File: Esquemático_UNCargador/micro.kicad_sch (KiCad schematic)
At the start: 14 parts, among them J2 Relay, Q1 PN2222A, Q2 PN2222A

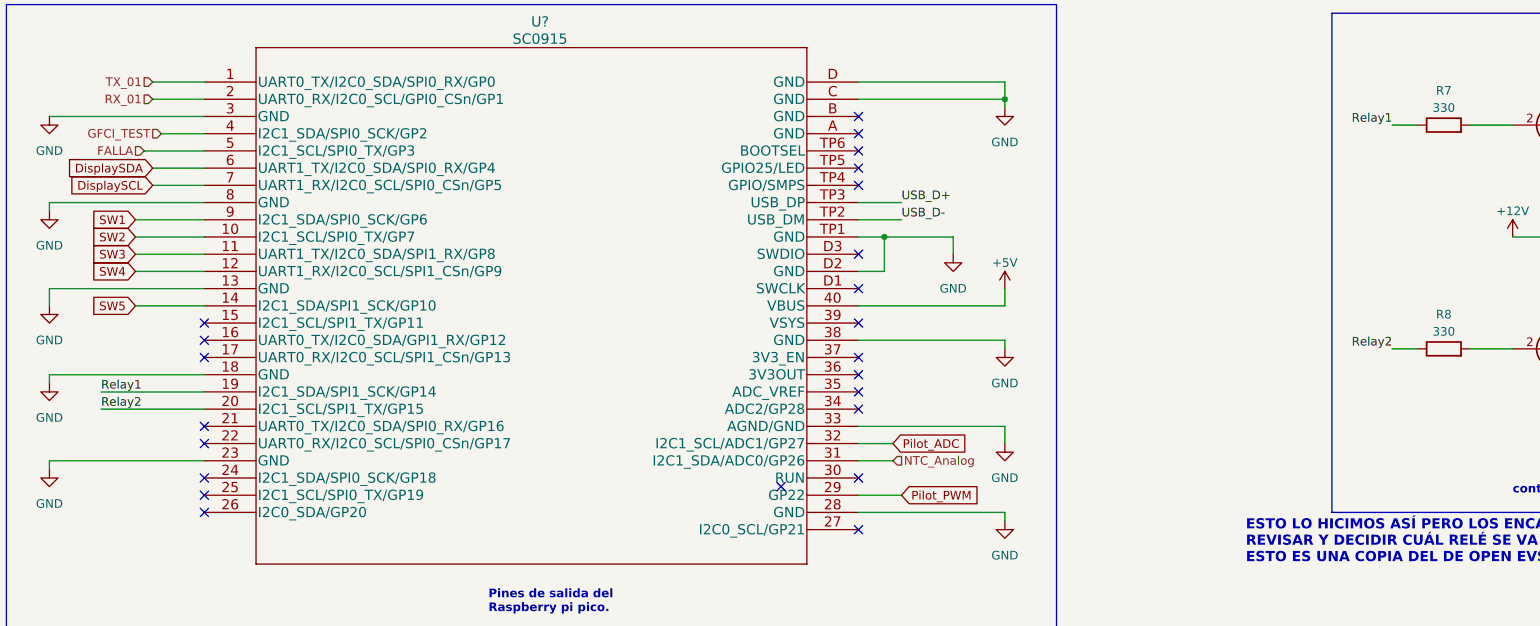
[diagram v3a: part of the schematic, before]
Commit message: Avances en Huellas
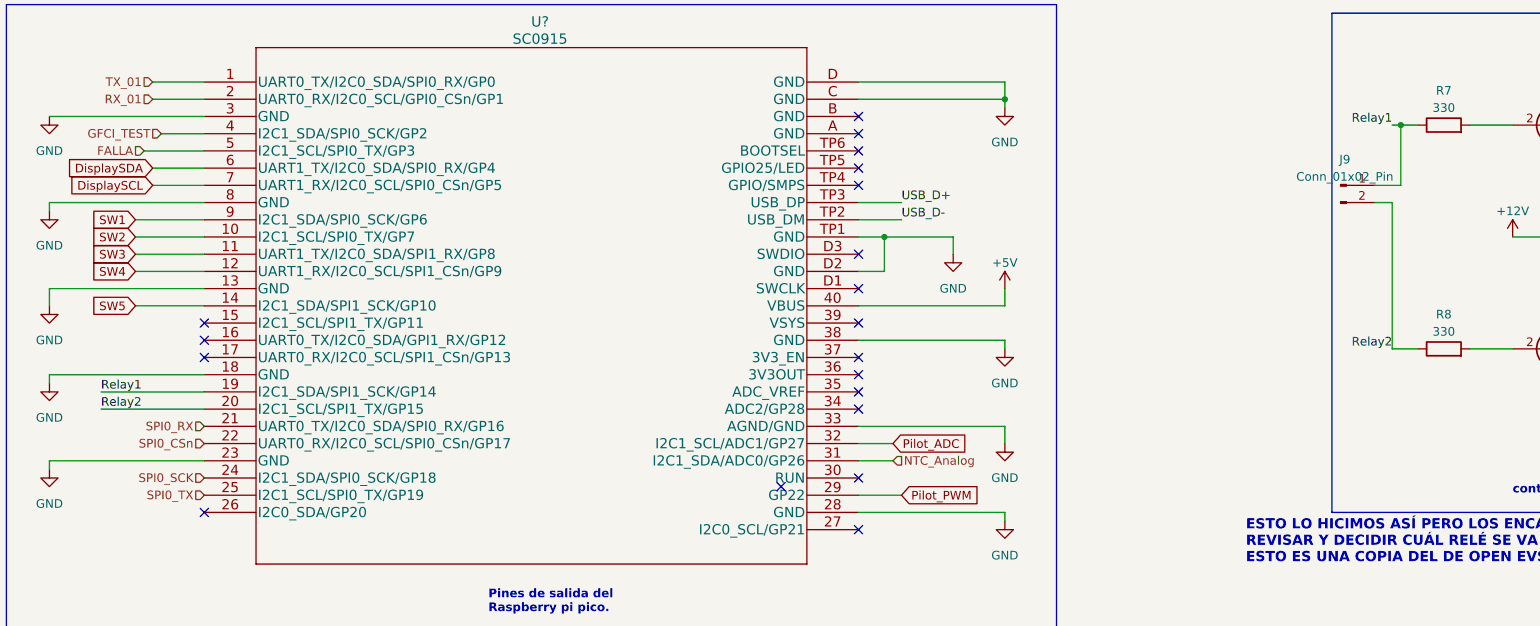
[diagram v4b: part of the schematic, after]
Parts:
- added J9: Conn_01x02_Pin, symbol Connector:Conn_01x02_Pin
- R7, R8: footprint (none) -> Resistor_THT:R_Axial_DIN0204_L3.6mm_D1.6mm_P5.08mm_Horizontal
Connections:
- net Relay1: now also J9.1 (Pin_1)
- net Relay2: now also J9.2 (Pin_2)
- net SPI0_RX: now reaches U?.21 (UART0_TX/I2C0_SDA/SPI0_RX/GP16)
- net SPI0_CSn: now reaches U?.22 (UART0_RX/I2C0_SCL/SPI0_CSn/GP17)
- net SPI0_SCK: now reaches U?.24 (I2C1_SDA/SPI0_SCK/GP18)
- net SPI0_TX: now reaches U?.25 (I2C1_SCL/SPI0_TX/GP19)
- no-connect marks 23 -> 19
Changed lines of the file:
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@@
   (junction (at 153.67 58.42) (diameter 0) (color 0 0 0 0)
+  )
+  (junction (at 229.87 41.91) (diameter 0) (color 0 0 0 0)
   )
   (junction (at 254 48.26) (diameter 0) (color 0 0 0 0)
@@
   (no_connect (at 149.86 48.26))
   (no_connect (at 53.34 76.2))
-  (no_connect (at 53.34 88.9))
   (no_connect (at 149.86 78.74))
   (no_connect (at 149.86 40.64))
   (no_connect (at 149.86 66.04))
   (no_connect (at 149.86 83.82))
-  (no_connect (at 53.34 86.36))
   (no_connect (at 149.86 76.2))
   (no_connect (at 149.86 81.28))
   (no_connect (at 53.34 99.06))
   (no_connect (at 149.86 60.96))
-  (no_connect (at 53.34 96.52))
   (no_connect (at 149.86 45.72))
   (no_connect (at 149.86 101.6))
@@
   (no_connect (at 149.86 50.8))
   (no_connect (at 149.86 93.98))
-  (no_connect (at 53.34 93.98))
   (no_connect (at 53.34 73.66))
   (no_connect (at 149.86 71.12))
@@
     (stroke (width 0) (type default))
   )
+  (wire (pts (xy 228.6 53.34) (xy 226.06 53.34))
+    (stroke (width 0) (type default))
+  )
   (wire (pts (xy 240.03 41.91) (xy 246.38 41.91))
     (stroke (width 0) (type default))
@@
     (stroke (width 0) (type default))
   )
+  (wire (pts (xy 228.6 74.93) (xy 228.6 53.34))
+    (stroke (width 0) (type default))
+  )
   (wire (pts (xy 269.24 55.88) (xy 269.24 48.26))
     (stroke (width 0) (type default))
@@
     (stroke (width 0) (type default))
   )
+  (wire (pts (xy 229.87 50.8) (xy 229.87 41.91))
+    (stroke (width 0) (type default))
+  )
   (wire (pts (xy 269.24 68.58) (xy 254 68.58))
     (stroke (width 0) (type default))
@@
     (stroke (width 0) (type default))
   )
+  (wire (pts (xy 226.06 50.8) (xy 229.87 50.8))
+    (stroke (width 0) (type default))
+  )
   (wire (pts (xy 171.45 99.06) (xy 171.45 100.33))
     (stroke (width 0) (type default))
@@
     (stroke (width 0) (type default))
   )
-  (wire (pts (xy 228.6 41.91) (xy 232.41 41.91))
+  (wire (pts (xy 228.6 41.91) (xy 229.87 41.91))
     (stroke (width 0) (type default))
   )
@@
   )
   (wire (pts (xy 115.57 152.4) (xy 118.11 152.4))
+    (stroke (width 0) (type default))
+  )
+  (wire (pts (xy 229.87 41.91) (xy 232.41 41.91))
     (stroke (width 0) (type default))
   )
@@
   )
   (hierarchical_label "RX_01" (shape input) (at 45.72 38.1 180) (fields_autoplaced)
+    (effects (font (size 1.27 1.27)) (justify right))
+  )
+  (hierarchical_label "SPI0_TX" (shape input) (at 53.34 96.52 180) (fields_autoplaced)
+    (effects (font (size 1.27 1.27)) (justify right))
+  )
+  (hierarchical_label "SPI0_SCK" (shape input) (at 53.34 93.98 180) (fields_autoplaced)
+    (effects (font (size 1.27 1.27)) (justify right))
+  )
+  (hierarchical_label "SPI0_CSn" (shape input) (at 53.34 88.9 180) (fields_autoplaced)
+    (effects (font (size 1.27 1.27)) (justify right))
+  )
+  (hierarchical_label "SPI0_RX" (shape input) (at 53.34 86.36 180) (fields_autoplaced)
     (effects (font (size 1.27 1.27)) (justify right))
   )
@@
       (effects (font (size 1.27 1.27)))
     )
-    (property "Footprint" "" (at 236.22 76.708 90)
+    (property "Footprint" "Resistor_THT:R_Axial_DIN0204_L3.6mm_D1.6mm_P5.08mm_Horizontal" (at 236.22 76.708 90)
       (effects (font (size 1.27 1.27)) hide)
     )
@@
       (effects (font (size 1.27 1.27)))
     )
-    (property "Footprint" "" (at 236.22 43.688 90)
+    (property "Footprint" "Resistor_THT:R_Axial_DIN0204_L3.6mm_D1.6mm_P5.08mm_Horizontal" (at 236.22 43.688 90)
       (effects (font (size 1.27 1.27)) hide)
     )
@@
         )
       )
+    )
+  )
+  (symbol (lib_id "Connector:Conn_01x02_Pin") (at 220.98 50.8 0) (unit 1)
+    (in_bom yes) (on_board yes) (dnp no) (fields_autoplaced)
+    (property "Reference" "J9" (at 221.615 46.99 0)
+      (effects (font (size 1.27 1.27)))
+    )
+    (property "Value" "Conn_01x02_Pin" (at 221.615 49.53 0)
+      (effects (font (size 1.27 1.27)))
+    )
+    (property "Footprint" "" (at 220.98 50.8 0)
+      (effects (font (size 1.27 1.27)) hide)
+    )
+    (property "Datasheet" "~" (at 220.98 50.8 0)
+      (effects (font (size 1.27 1.27)) hide)
+    )
+    (pin "1")
+    (pin "2")
+    (instances
+      (project "CircuitoPotencia"
+        (path "/f64e4c48-29c2-4644-b6e3-d55b9152fc29/27c27843-11c4-470f-a3f9-e81d775d20fc"
+          (reference "J9") (unit 1)
+        )
+      )

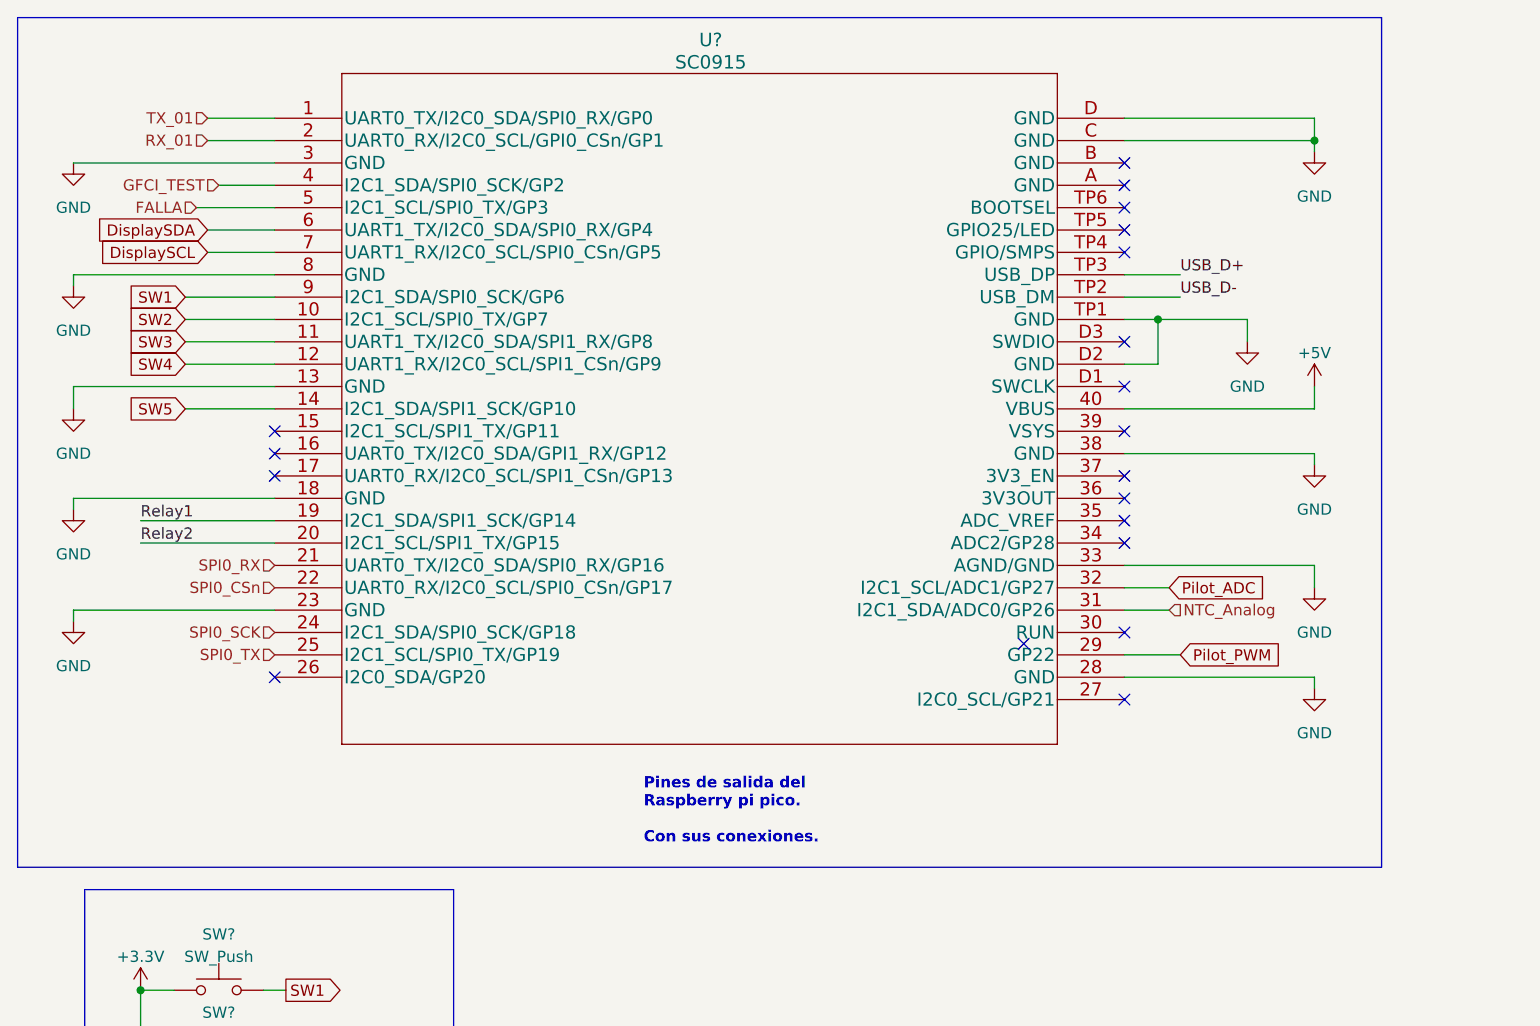
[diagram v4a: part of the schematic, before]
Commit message: Modificación de la huella del microcontrolador
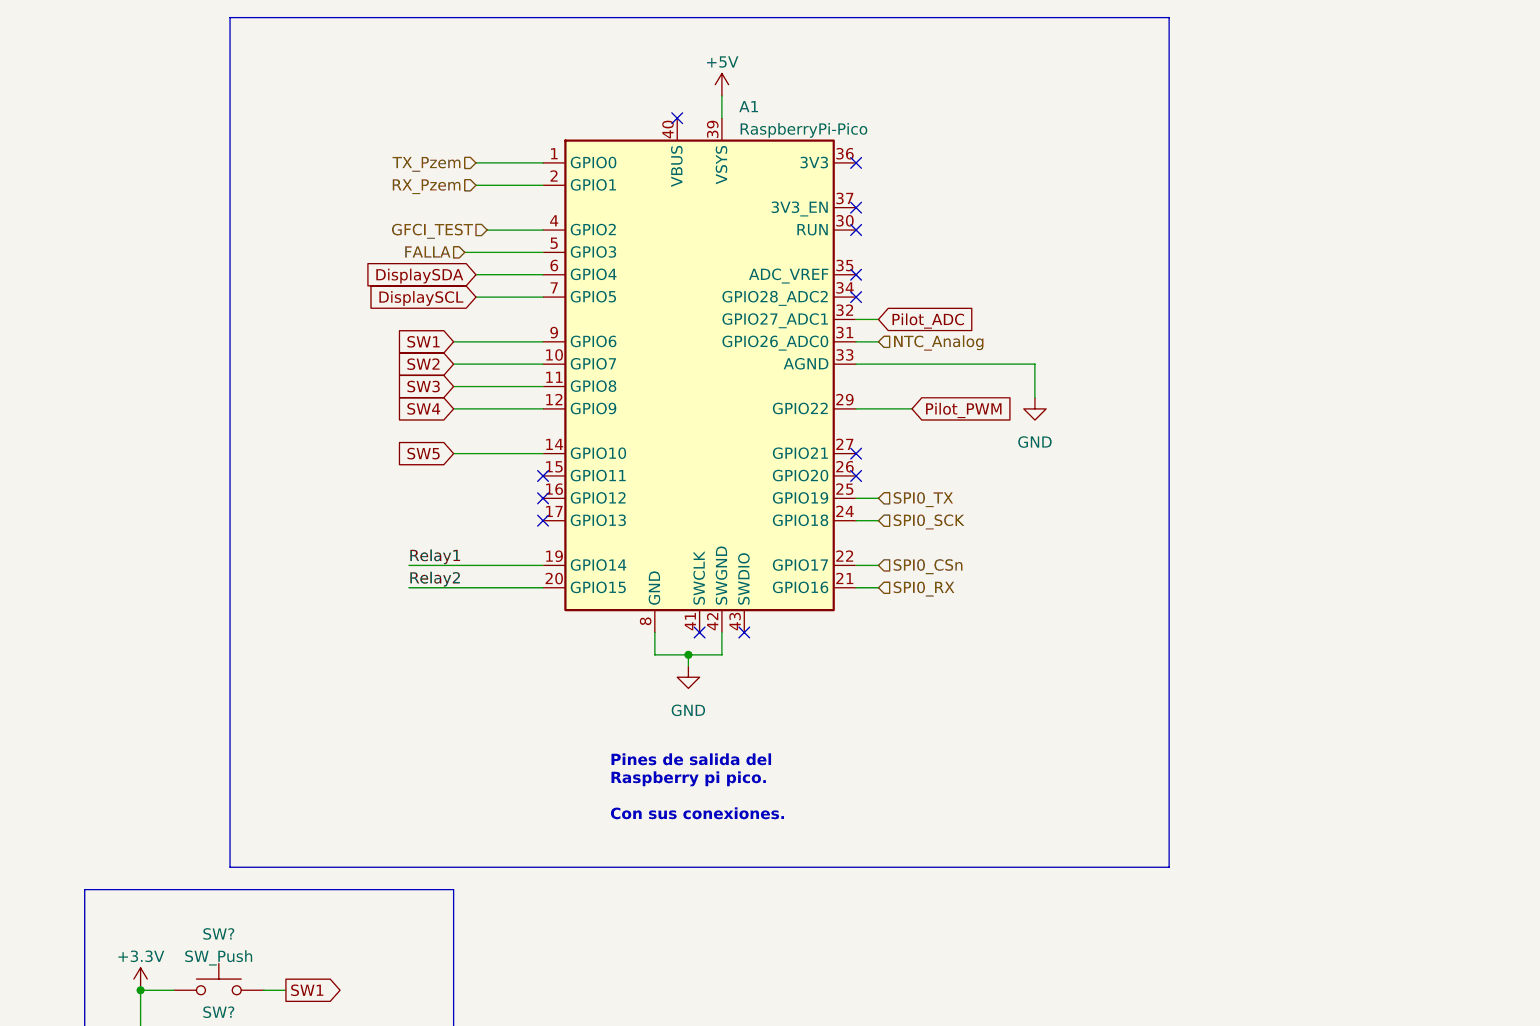
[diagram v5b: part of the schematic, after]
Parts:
- removed U?: SC0915, RP2040:RP2040_SC0915, symbol RP2040:SC0915
- added A1: RaspberryPi-Pico, ModulePico:Raspberry_Pi_Pico_SMT_THT, symbol MCU_ModulePico:RaspberryPi-Pico
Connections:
- net +5V: now also A1.39 (VSYS)
- net DisplaySCL: now also A1.7 (GPIO5)
- net DisplaySDA: now also A1.6 (GPIO4)
- net FALLA: now also A1.5 (GPIO3)
- net GFCI_TEST: now also A1.4 (GPIO2)
- net GND: now also A1.13 (GND), A1.18 (GND), A1.23 (GND), A1.28 (GND), A1.3 (GND), A1.33 (AGND), A1.38 (GND), A1.42 (SWGND), A1.8 (GND)
- net NTC_Analog: now also A1.31 (GPIO26_ADC0)
- net Pilot_ADC: now also A1.32 (GPIO27_ADC1)
- net Pilot_PWM: now also A1.29 (GPIO22)
- net Relay1: now also A1.19 (GPIO14)
- net Relay2: now also A1.20 (GPIO15)
- net SPI0_CSn: now also A1.22 (GPIO17)
- net SPI0_RX: now also A1.21 (GPIO16)
- net SPI0_SCK: now also A1.24 (GPIO18)
- net SPI0_TX: now also A1.25 (GPIO19)
- net SW1: now also A1.9 (GPIO6)
- net SW2: now also A1.10 (GPIO7)
- net SW3: now also A1.11 (GPIO8)
- net SW4: now also A1.12 (GPIO9)
- net SW5: now also A1.14 (GPIO10)
- new net RX_Pzem: A1.2 (GPIO1)
- new net TX_Pzem: A1.1 (GPIO0)
- no-connect marks 19 -> 13

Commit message: Modificación relays
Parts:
- removed J2: Relay, symbol Connector:Conn_01x03_Socket
- removed J9: Conn_01x02_Pin, symbol Connector:Conn_01x02_Pin
- added C6, C7: 100uF, Capacitor_THT:CP_Radial_D8.0mm_P3.50mm, symbol Device:C_Polarized
- added J2: Relay1, Connector_Molex:Molex_KK-254_AE-6410-02A_1x02_P2.54mm_Vertical, symbol Connector:Conn_01x02_Socket
- added J9: Relay2, Connector_Molex:Molex_KK-254_AE-6410-02A_1x02_P2.54mm_Vertical, symbol Connector:Conn_01x02_Socket
- added R20, R21: 47, Resistor_THT:R_Axial_DIN0207_L6.3mm_D2.5mm_P10.16mm_Horizontal, symbol Device:R
- R7, R8: footprint Resistor_THT:R_Axial_DIN0204_L3.6mm_D1.6mm_P5.08mm_Horizontal -> Resistor_THT:R_Axial_DIN0207_L6.3mm_D2.5mm_P10.16mm_Horizontal
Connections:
- net +5V: now also R20.1, R21.1
- net GND: now also C6.2, C7.2
- net at R8.2: now also Q1.2 (B); no longer Q2.2 (B)
- net at R7.2: now also Q2.2 (B); no longer Q1.2 (B)
- net at D4.2 (A), Q2.3 (C): now also J2.2 (Pin_2)
- net at D3.2 (A), Q1.3 (C): now also J9.1 (Pin_1)
- net +12V: no longer names the net of D3.1 (K)
- net +12V: now also C7.1, J9.2 (Pin_2), R21.2; no longer D4.1 (K)
- net Relay1 renamed Relay1_ctr
- net Relay2 renamed Relay2_ctr
- new net: C6.1, D4.1 (K), J2.1 (Pin_1), R20.2
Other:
- note removed: "ESTO LO HICIMOS ASÍ PERO LOS ENCARGADOS POR FAVOR VERIFICAR SI ESTÁN DE ACUERDO REVISAR Y DECIDIR CUÁL RELÉ SE VA A UASR PORQUE DEPENDIENDO DE ESO TOCA CAMBIAR ESTO ES UNA COPIA DEL DE OPEN EVSE"
- moved on the sheet: A1, J?, R7, R8, SW?

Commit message: Cambios de recomendaciones profesor
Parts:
- J?: footprint (none) -> Connector_PinHeader_2.54mm:PinHeader_1x08_P2.54mm_Vertical
- SW? (x5): footprint (none) -> Connector_PinHeader_2.54mm:PinHeader_1x02_P2.54mm_Vertical
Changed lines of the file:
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@@
       (effects (font (size 1.27 1.27)))
     )
-    (property "Footprint" "" (at 52.07 149.86 0)
+    (property "Footprint" "Connector_PinHeader_2.54mm:PinHeader_1x02_P2.54mm_Vertical" (at 52.07 149.86 0)
       (effects (font (size 1.27 1.27)) hide)
     )
@@
       (effects (font (size 1.27 1.27)))
     )
-    (property "Footprint" "" (at 52.07 167.64 0)
+    (property "Footprint" "Connector_PinHeader_2.54mm:PinHeader_1x02_P2.54mm_Vertical" (at 52.07 167.64 0)
       (effects (font (size 1.27 1.27)) hide)
     )
@@
       (effects (font (size 1.27 1.27)))
     )
-    (property "Footprint" "" (at 52.07 176.53 0)
+    (property "Footprint" "Connector_PinHeader_2.54mm:PinHeader_1x02_P2.54mm_Vertical" (at 52.07 176.53 0)
       (effects (font (size 1.27 1.27)) hide)
     )
@@
       (effects (font (size 1.27 1.27)))
     )
-    (property "Footprint" "" (at 52.07 158.75 0)
+    (property "Footprint" "Connector_PinHeader_2.54mm:PinHeader_1x02_P2.54mm_Vertical" (at 52.07 158.75 0)
       (effects (font (size 1.27 1.27)) hide)
     )
@@
       (effects (font (size 1.27 1.27)))
     )
-    (property "Footprint" "" (at 52.07 140.97 0)
+    (property "Footprint" "Connector_PinHeader_2.54mm:PinHeader_1x02_P2.54mm_Vertical" (at 52.07 140.97 0)
       (effects (font (size 1.27 1.27)) hide)
     )
@@
       (effects (font (size 1.27 1.27)))
     )
-    (property "Footprint" "" (at 115.57 171.45 0)
-      (effects (font (size 1.27 1.27)) hide)
-    )
+    (property "Footprint" "Connector_PinHeader_2.54mm:PinHeader_1x08_P2.54mm_Vertical" (at 115.57 171.45 0)
+      (effects (font (size 1.27 1.27)) hide)
+    )
